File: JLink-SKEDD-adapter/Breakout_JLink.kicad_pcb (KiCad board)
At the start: 2 copper layers, 27.4 x 26 mm, 7 parts, among them J1 UART_ClientSide, J2 Conn_02x10_Odd_Even, J3 Jitter_Debug_HostSide, J4 Conn_01x06_Female

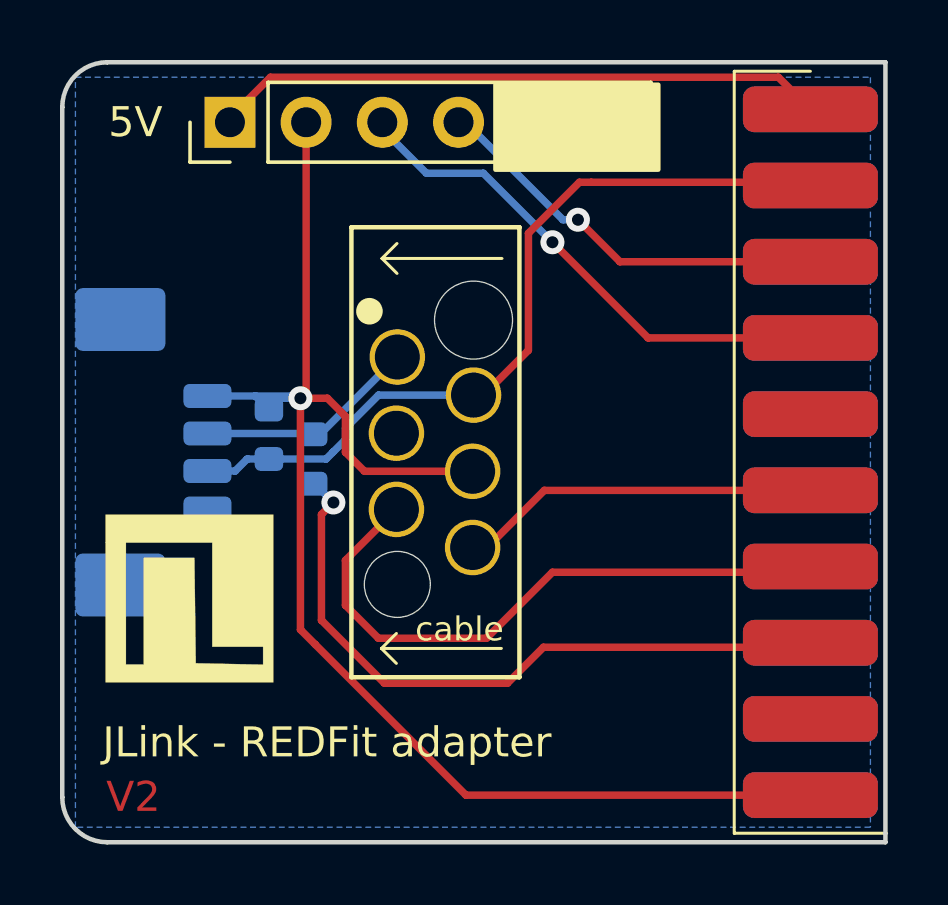
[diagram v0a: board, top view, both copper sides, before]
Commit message: Update JLink SKEDD breakout to Kicad 10
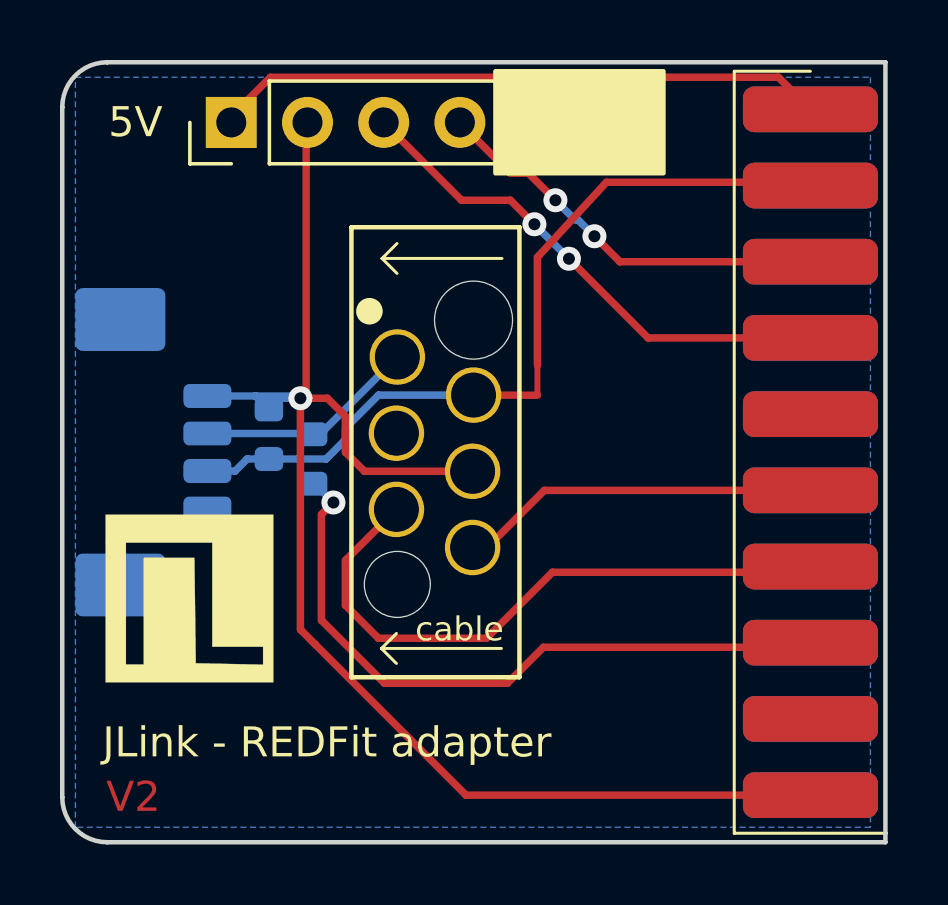
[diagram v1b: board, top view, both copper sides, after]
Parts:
- added NT1: NetTie_2, Jitter_Footprints:NetTie-2_SMD_Pad0.2mm, F.Cu at (190.9, 82.6)
- J2: value Conn_02x10_Odd_Even -> 2x10 female header 2.56mm pitch. With a notch/key on top side
- J4: value Conn_01x06_Female -> Conn_01x06_Socket
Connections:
- net Net-(J1-RX_(client)) renamed /RX_client
- J1 pad 2: /Rx_JLink -> /TX_client
- J2 pad 14: unconnected-(J2-Pin_14-Pad14) -> GND
- J2 pad 16: unconnected-(J2-Pin_16-Pad16) -> GND
- J2 pad 18: unconnected-(J2-Pin_18-Pad18) -> GND
- J2 pad 20: unconnected-(J2-Pin_20-Pad20) -> GND
- J3 pad 2: /Rx_JLink -> /TX_client
- R2 pad 2: /Rx_JLink -> /TX_client
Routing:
- net /Rx_JLink: track 26.6 -> 13.8 mm
- net /TX_client: track 0.00 -> 12.6 mm
- net /SWO: track 17.3 -> 17.7 mm, vias 1 -> 2
- net /nRESET: track 13.4 -> 13.6 mm, vias 1 -> 2
